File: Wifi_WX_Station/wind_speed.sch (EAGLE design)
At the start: 8 parts, among them T1 MMBT3904

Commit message: updated BOM with all prices- As Checked in to BATCH PCB
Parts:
- +5V, GND, OUT: value LSP10 -> TPSOL; device solpad:LSP10 -> wifi_WX:TPSOL
- OPTO1: device 1AA_Stofer:OSRAM_SHF9201 -> wifi_WX:OSRAM_SHF9201
- R1: device rcl:R-US_R0805 -> rcl:R-US_R0603
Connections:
- net N$2: now also GND.P$1; no longer GND.MP
- net N$3: now also +5V.P$1; no longer +5V.MP
- net N$4: now also OUT.P$1; no longer OUT.MP
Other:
- moved on the sheet: R1, R2, R3, T1
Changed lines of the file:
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@@
 </classes>
 <parts>
-<part name="OPTO1" library="1AA_Stofer" deviceset="OSRAM_SHF9201" device=""/>
+<part name="OPTO1" library="wifi_WX" deviceset="OSRAM_SHF9201" device=""/>
 <part name="T1" library="transistor" deviceset="BC846" device="" value="MMBT3904"/>
-<part name="R1" library="rcl" deviceset="R-US_" device="R0805" value="10K"/>
-<part name="+5V" library="solpad" deviceset="LSP10" device=""/>
-<part name="GND" library="solpad" deviceset="LSP10" device=""/>
-<part name="OUT" library="solpad" deviceset="LSP10" device=""/>
+<part name="R1" library="rcl" deviceset="R-US_" device="R0603" value="10K"/>
 <part name="R2" library="rcl" deviceset="R-US_" device="R0603" value="120o"/>
 <part name="R3" library="rcl" deviceset="R-US_" device="R0603" value="120o"/>
+<part name="+5V" library="wifi_WX" deviceset="TP" device="SOL"/>
+<part name="GND" library="wifi_WX" deviceset="TP" device="SOL"/>
+<part name="OUT" library="wifi_WX" deviceset="TP" device="SOL"/>
 </parts>
 <sheets>
@@
 </plain>
 <instances>
-<instance part="OPTO1" gate="G$1" x="101.6" y="60.96"/>
-<instance part="T1" gate="G$1" x="139.7" y="63.5"/>
-<instance part="R1" gate="G$1" x="116.84" y="81.28" rot="R90"/>
-<instance part="+5V" gate="1" x="83.82" y="88.9" rot="R90"/>
-<instance part="GND" gate="1" x="83.82" y="48.26" rot="R90"/>
-<instance part="OUT" gate="1" x="142.24" y="86.36"/>
-<instance part="R2" gate="G$1" x="91.44" y="83.82" rot="R90"/>
-<instance part="R3" gate="G$1" x="91.44" y="73.66" rot="R90"/>
+<instance part="OPTO1" gate="G$1" x="101.6" y="60.96" smashed="yes">
+<attribute name="NAME" x="99.06" y="63.5" size="1.27" layer="95"/>
+<attribute name="VALUE" x="96.52" y="50.8" size="1.27" layer="96"/>
+</instance>
+<instance part="T1" gate="G$1" x="124.46" y="71.12"/>
+<instance part="R1" gate="G$1" x="109.22" y="83.82" rot="R90"/>
+<instance part="R2" gate="G$1" x="96.52" y="91.44" rot="R90"/>
+<instance part="R3" gate="G$1" x="96.52" y="78.74" rot="R90"/>
+<instance part="+5V" gate="G$1" x="83.82" y="96.52"/>
+<instance part="GND" gate="G$1" x="83.82" y="48.26"/>
+<instance part="OUT" gate="G$1" x="132.08" y="96.52" rot="R180"/>
 </instances>
 <busses>
@@
 <pinref part="R1" gate="G$1" pin="1"/>
 <pinref part="OPTO1" gate="G$1" pin="C"/>
-<wire x1="116.84" y1="76.2" x2="116.84" y2="68.58" width="0.1524" layer="91"/>
-<wire x1="116.84" y1="68.58" x2="111.76" y2="68.58" width="0.1524" layer="91"/>
-<wire x1="111.76" y1="68.58" x2="124.46" y2="68.58" width="0.1524" layer="91"/>
-<wire x1="124.46" y1="68.58" x2="124.46" y2="63.5" width="0.1524" layer="91"/>
+<wire x1="109.22" y1="78.74" x2="109.22" y2="71.12" width="0.1524" layer="91"/>
+<wire x1="109.22" y1="71.12" x2="121.92" y2="71.12" width="0.1524" layer="91"/>
 <pinref part="T1" gate="G$1" pin="B"/>
-<wire x1="124.46" y1="63.5" x2="137.16" y2="63.5" width="0.1524" layer="91"/>
 </segment>
 </net>
@@
 <segment>
 <pinref part="OPTO1" gate="G$1" pin="E"/>
-<wire x1="111.76" y1="55.88" x2="111.76" y2="48.26" width="0.1524" layer="91"/>
+<wire x1="109.22" y1="53.34" x2="109.22" y2="48.26" width="0.1524" layer="91"/>
 <pinref part="T1" gate="G$1" pin="E"/>
-<wire x1="111.76" y1="48.26" x2="142.24" y2="48.26" width="0.1524" layer="91"/>
-<wire x1="142.24" y1="48.26" x2="142.24" y2="58.42" width="0.1524" layer="91"/>
+<wire x1="109.22" y1="48.26" x2="127" y2="48.26" width="0.1524" layer="91"/>
+<wire x1="127" y1="48.26" x2="127" y2="66.04" width="0.1524" layer="91"/>
 <pinref part="OPTO1" gate="G$1" pin="CATH"/>
-<wire x1="111.76" y1="48.26" x2="86.36" y2="48.26" width="0.1524" layer="91"/>
-<wire x1="86.36" y1="48.26" x2="86.36" y2="55.88" width="0.1524" layer="91"/>
-<wire x1="86.36" y1="55.88" x2="93.98" y2="55.88" width="0.1524" layer="91"/>
-<pinref part="GND" gate="1" pin="MP"/>
-<junction x="86.36" y="48.26"/>
+<wire x1="109.22" y1="48.26" x2="96.52" y2="48.26" width="0.1524" layer="91"/>
+<wire x1="88.9" y1="48.26" x2="96.52" y2="48.26" width="0.1524" layer="91"/>
+<wire x1="96.52" y1="48.26" x2="96.52" y2="53.34" width="0.1524" layer="91"/>
+<pinref part="GND" gate="G$1" pin="P$1"/>
 </segment>
 </net>
 <net name="N$3" class="0">
 <segment>
-<wire x1="86.36" y1="88.9" x2="91.44" y2="88.9" width="0.1524" layer="91"/>
+<wire x1="88.9" y1="96.52" x2="96.52" y2="96.52" width="0.1524" layer="91"/>
 <pinref part="R1" gate="G$1" pin="2"/>
-<wire x1="91.44" y1="88.9" x2="116.84" y2="88.9" width="0.1524" layer="91"/>
-<wire x1="116.84" y1="88.9" x2="116.84" y2="86.36" width="0.1524" layer="91"/>
-<pinref part="+5V" gate="1" pin="MP"/>
+<wire x1="96.52" y1="96.52" x2="109.22" y2="96.52" width="0.1524" layer="91"/>
+<wire x1="109.22" y1="96.52" x2="109.22" y2="88.9" width="0.1524" layer="91"/>
 <pinref part="R2" gate="G$1" pin="2"/>
+<pinref part="+5V" gate="G$1" pin="P$1"/>
 </segment>
 </net>
@@
 <segment>
 <pinref part="T1" gate="G$1" pin="C"/>
-<wire x1="142.24" y1="68.58" x2="142.24" y2="83.82" width="0.1524" layer="91"/>
-<pinref part="OUT" gate="1" pin="MP"/>
+<wire x1="127" y1="76.2" x2="127" y2="96.52" width="0.1524" layer="91"/>
+<pinref part="OUT" gate="G$1" pin="P$1"/>
 </segment>
 </net>
@@
 <segment>
 <pinref part="OPTO1" gate="G$1" pin="AN"/>
-<wire x1="91.44" y1="68.58" x2="93.98" y2="68.58" width="0.1524" layer="91"/>
+<wire x1="96.52" y1="73.66" x2="96.52" y2="71.12" width="0.1524" layer="91"/>
 <pinref part="R3" gate="G$1" pin="1"/>
 </segment>
@@
 <pinref part="R2" gate="G$1" pin="1"/>
 <pinref part="R3" gate="G$1" pin="2"/>
+<wire x1="96.52" y1="86.36" x2="96.52" y2="83.82" width="0.1524" layer="91"/>
 </segment>
 </net>

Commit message: Revision B.1
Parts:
- added R4: 1K, rcl:R-US_R0603
- added R5: 330, rcl:R-US_R0603
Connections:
- net N$3: now also R4.2
- net N$4: now also R4.1, R5.1
- net N$6: now also R5.2
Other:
- moved on the sheet: +5V, OUT, R1, R2, R3
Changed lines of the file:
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@@
 <part name="GND" library="wifi_WX" deviceset="TP" device="SOL"/>
 <part name="OUT" library="wifi_WX" deviceset="TP" device="SOL"/>
+<part name="R4" library="rcl" deviceset="R-US_" device="R0603" value="1K"/>
+<part name="R5" library="rcl" deviceset="R-US_" device="R0603" value="330"/>
 </parts>
 <sheets>
@@
 </instance>
 <instance part="T1" gate="G$1" x="124.46" y="71.12"/>
-<instance part="R1" gate="G$1" x="109.22" y="83.82" rot="R90"/>
-<instance part="R2" gate="G$1" x="96.52" y="91.44" rot="R90"/>
-<instance part="R3" gate="G$1" x="96.52" y="78.74" rot="R90"/>
-<instance part="+5V" gate="G$1" x="83.82" y="96.52"/>
+<instance part="R1" gate="G$1" x="109.22" y="96.52" rot="R90"/>
+<instance part="R2" gate="G$1" x="96.52" y="99.06" rot="R90"/>
+<instance part="R3" gate="G$1" x="96.52" y="76.2" rot="R90"/>
+<instance part="+5V" gate="G$1" x="83.82" y="104.14"/>
 <instance part="GND" gate="G$1" x="83.82" y="48.26"/>
-<instance part="OUT" gate="G$1" x="132.08" y="96.52" rot="R180"/>
+<instance part="OUT" gate="G$1" x="132.08" y="104.14" rot="R180"/>
+<instance part="R4" gate="G$1" x="116.84" y="104.14" rot="R180"/>
+<instance part="R5" gate="G$1" x="119.38" y="86.36" rot="R180"/>
 </instances>
 <busses>
@@
 <pinref part="R1" gate="G$1" pin="1"/>
 <pinref part="OPTO1" gate="G$1" pin="C"/>
-<wire x1="109.22" y1="78.74" x2="109.22" y2="71.12" width="0.1524" layer="91"/>
+<wire x1="109.22" y1="91.44" x2="109.22" y2="71.12" width="0.1524" layer="91"/>
 <wire x1="109.22" y1="71.12" x2="121.92" y2="71.12" width="0.1524" layer="91"/>
 <pinref part="T1" gate="G$1" pin="B"/>
@@
 <net name="N$3" class="0">
 <segment>
-<wire x1="88.9" y1="96.52" x2="96.52" y2="96.52" width="0.1524" layer="91"/>
+<wire x1="88.9" y1="104.14" x2="96.52" y2="104.14" width="0.1524" layer="91"/>
 <pinref part="R1" gate="G$1" pin="2"/>
-<wire x1="96.52" y1="96.52" x2="109.22" y2="96.52" width="0.1524" layer="91"/>
-<wire x1="109.22" y1="96.52" x2="109.22" y2="88.9" width="0.1524" layer="91"/>
+<wire x1="96.52" y1="104.14" x2="109.22" y2="104.14" width="0.1524" layer="91"/>
+<wire x1="109.22" y1="104.14" x2="109.22" y2="101.6" width="0.1524" layer="91"/>
 <pinref part="R2" gate="G$1" pin="2"/>
 <pinref part="+5V" gate="G$1" pin="P$1"/>
+<pinref part="R4" gate="G$1" pin="2"/>
+<wire x1="109.22" y1="104.14" x2="111.76" y2="104.14" width="0.1524" layer="91"/>
 </segment>
 </net>
@@
 <segment>
 <pinref part="T1" gate="G$1" pin="C"/>
-<wire x1="127" y1="76.2" x2="127" y2="96.52" width="0.1524" layer="91"/>
+<wire x1="127" y1="76.2" x2="127" y2="86.36" width="0.1524" layer="91"/>
 <pinref part="OUT" gate="G$1" pin="P$1"/>
+<pinref part="R4" gate="G$1" pin="1"/>
+<wire x1="127" y1="86.36" x2="127" y2="104.14" width="0.1524" layer="91"/>
+<wire x1="121.92" y1="104.14" x2="127" y2="104.14" width="0.1524" layer="91"/>
+<pinref part="R5" gate="G$1" pin="1"/>
+<wire x1="124.46" y1="86.36" x2="127" y2="86.36" width="0.1524" layer="91"/>
 </segment>
 </net>
@@
 <segment>
 <pinref part="OPTO1" gate="G$1" pin="AN"/>
-<wire x1="96.52" y1="73.66" x2="96.52" y2="71.12" width="0.1524" layer="91"/>
 <pinref part="R3" gate="G$1" pin="1"/>
 </segment>
@@
 <pinref part="R2" gate="G$1" pin="1"/>
 <pinref part="R3" gate="G$1" pin="2"/>
-<wire x1="96.52" y1="86.36" x2="96.52" y2="83.82" width="0.1524" layer="91"/>
+<wire x1="96.52" y1="93.98" x2="96.52" y2="86.36" width="0.1524" layer="91"/>
+<pinref part="R5" gate="G$1" pin="2"/>
+<wire x1="96.52" y1="86.36" x2="96.52" y2="81.28" width="0.1524" layer="91"/>
+<wire x1="114.3" y1="86.36" x2="96.52" y2="86.36" width="0.1524" layer="91"/>
 </segment>
 </net>

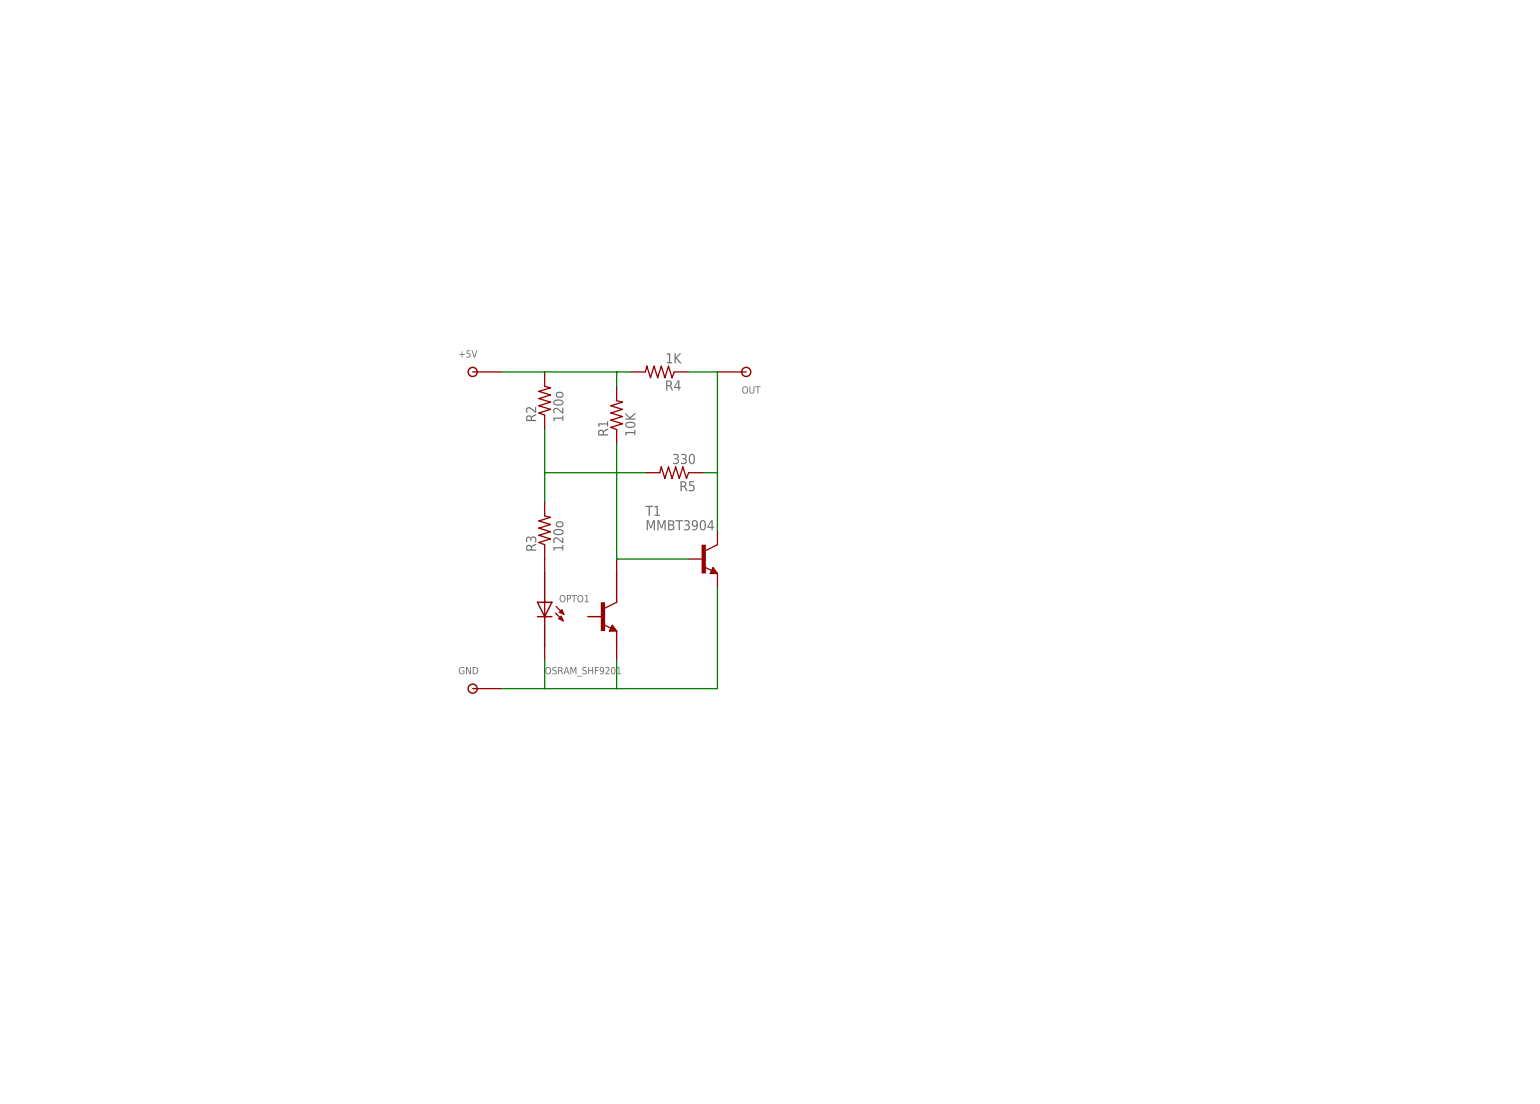
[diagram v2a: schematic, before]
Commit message: added SILabs Hygrometer board Added frames to the schematics
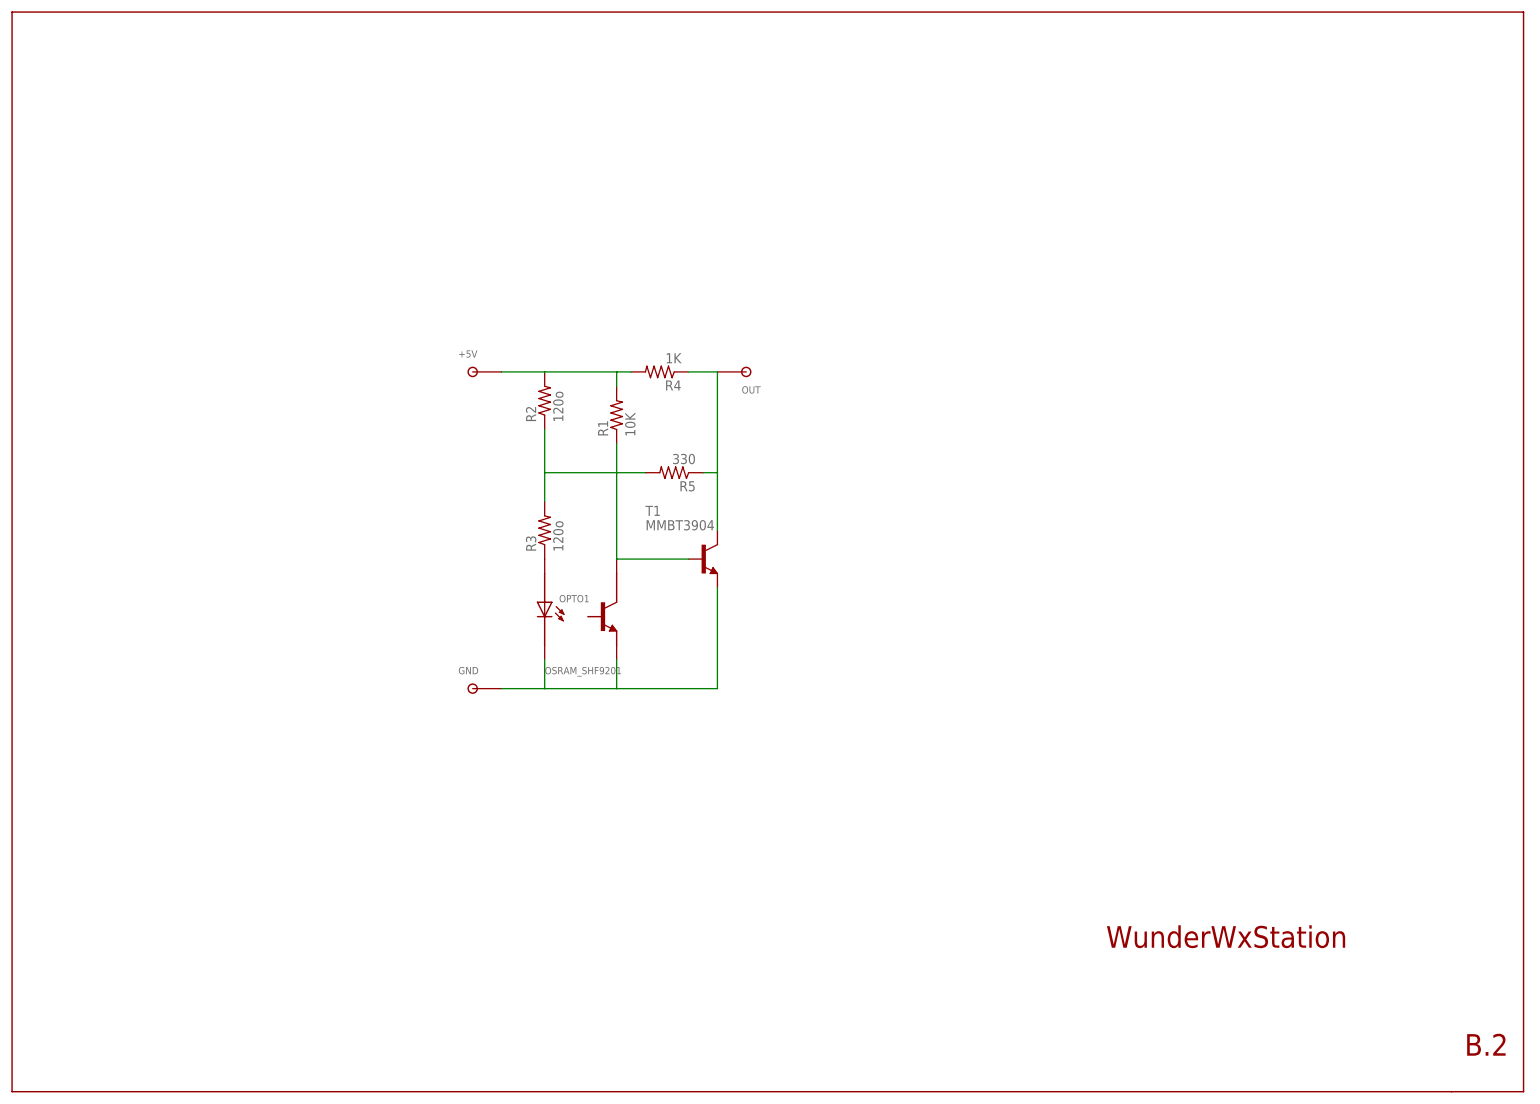
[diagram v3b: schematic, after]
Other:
- note added: "B.2"
- note added: "WunderWxStation"
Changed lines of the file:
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@@
 <grid distance="0.1" unitdist="inch" unit="inch" style="lines" multiple="1" display="no" altdistance="0.01" altunitdist="inch" altunit="inch"/>
 <layers>
-<layer number="1" name="Top" color="4" fill="1" visible="yes" active="no"/>
-<layer number="16" name="Bottom" color="1" fill="1" visible="yes" active="no"/>
-<layer number="17" name="Pads" color="2" fill="1" visible="yes" active="no"/>
-<layer number="18" name="Vias" color="2" fill="1" visible="yes" active="no"/>
-<layer number="19" name="Unrouted" color="6" fill="1" visible="yes" active="no"/>
-<layer number="20" name="Dimension" color="15" fill="1" visible="yes" active="no"/>
-<layer number="21" name="tPlace" color="7" fill="1" visible="yes" active="no"/>
-<layer number="22" name="bPlace" color="7" fill="1" visible="yes" active="no"/>
-<layer number="23" name="tOrigins" color="15" fill="1" visible="yes" active="no"/>
-<layer number="24" name="bOrigins" color="15" fill="1" visible="yes" active="no"/>
-<layer number="25" name="tNames" color="7" fill="1" visible="yes" active="no"/>
-<layer number="26" name="bNames" color="7" fill="1" visible="yes" active="no"/>
-<layer number="27" name="tValues" color="7" fill="1" visible="yes" active="no"/>
-<layer number="28" name="bValues" color="7" fill="1" visible="yes" active="no"/>
+<layer number="1" name="Top" color="4" fill="1" visible="no" active="no"/>
+<layer number="16" name="Bottom" color="1" fill="1" visible="no" active="no"/>
+<layer number="17" name="Pads" color="2" fill="1" visible="no" active="no"/>
+<layer number="18" name="Vias" color="2" fill="1" visible="no" active="no"/>
+<layer number="19" name="Unrouted" color="6" fill="1" visible="no" active="no"/>
+<layer number="20" name="Dimension" color="15" fill="1" visible="no" active="no"/>
+<layer number="21" name="tPlace" color="7" fill="1" visible="no" active="no"/>
+<layer number="22" name="bPlace" color="7" fill="1" visible="no" active="no"/>
+<layer number="23" name="tOrigins" color="15" fill="1" visible="no" active="no"/>
+<layer number="24" name="bOrigins" color="15" fill="1" visible="no" active="no"/>
+<layer number="25" name="tNames" color="7" fill="1" visible="no" active="no"/>
+<layer number="26" name="bNames" color="7" fill="1" visible="no" active="no"/>
+<layer number="27" name="tValues" color="7" fill="1" visible="no" active="no"/>
+<layer number="28" name="bValues" color="7" fill="1" visible="no" active="no"/>
 <layer number="29" name="tStop" color="7" fill="3" visible="no" active="no"/>
 <layer number="30" name="bStop" color="7" fill="6" visible="no" active="no"/>
@@
 <layer number="35" name="tGlue" color="7" fill="4" visible="no" active="no"/>
 <layer number="36" name="bGlue" color="7" fill="5" visible="no" active="no"/>
-<layer number="37" name="tTest" color="7" fill="1" visible="yes" active="no"/>
-<layer number="38" name="bTest" color="7" fill="1" visible="yes" active="no"/>
+<layer number="37" name="tTest" color="7" fill="1" visible="no" active="no"/>
+<layer number="38" name="bTest" color="7" fill="1" visible="no" active="no"/>
 <layer number="39" name="tKeepout" color="4" fill="11" visible="no" active="no"/>
 <layer number="40" name="bKeepout" color="1" fill="11" visible="no" active="no"/>
@@
 <layer number="44" name="Drills" color="7" fill="1" visible="no" active="no"/>
 <layer number="45" name="Holes" color="7" fill="1" visible="no" active="no"/>
-<layer number="46" name="Milling" color="3" fill="1" visible="yes" active="no"/>
-<layer number="47" name="Measures" color="7" fill="1" visible="yes" active="no"/>
-<layer number="48" name="Document" color="7" fill="1" visible="yes" active="no"/>
-<layer number="49" name="Reference" color="7" fill="1" visible="yes" active="no"/>
-<layer number="50" name="dxf" color="7" fill="1" visible="yes" active="no"/>
-<layer number="51" name="tDocu" color="7" fill="1" visible="yes" active="no"/>
-<layer number="52" name="bDocu" color="7" fill="1" visible="yes" active="no"/>
-<layer number="53" name="tGND_GNDA" color="7" fill="9" visible="yes" active="no"/>
-<layer number="54" name="bGND_GNDA" color="1" fill="9" visible="yes" active="no"/>
-<layer number="56" name="wert" color="7" fill="1" visible="yes" active="no"/>
+<layer number="46" name="Milling" color="3" fill="1" visible="no" active="no"/>
+<layer number="47" name="Measures" color="7" fill="1" visible="no" active="no"/>
+<layer number="48" name="Document" color="7" fill="1" visible="no" active="no"/>
+<layer number="49" name="Reference" color="7" fill="1" visible="no" active="no"/>
+<layer number="50" name="dxf" color="7" fill="1" visible="no" active="no"/>
+<layer number="51" name="tDocu" color="7" fill="1" visible="no" active="no"/>
+<layer number="52" name="bDocu" color="7" fill="1" visible="no" active="no"/>
+<layer number="53" name="tGND_GNDA" color="7" fill="9" visible="no" active="no"/>
+<layer number="54" name="bGND_GNDA" color="1" fill="9" visible="no" active="no"/>
+<layer number="56" name="wert" color="7" fill="1" visible="no" active="no"/>
 <layer number="91" name="Nets" color="2" fill="1" visible="yes" active="yes"/>
 <layer number="92" name="Busses" color="1" fill="1" visible="yes" active="yes"/>
@@
 <part name="R4" library="rcl" deviceset="R-US_" device="R0603" value="1K"/>
 <part name="R5" library="rcl" deviceset="R-US_" device="R0603" value="330"/>
+<part name="U$1" library="1AA_Stofer" deviceset="8.5X11" device=""/>
 </parts>
 <sheets>
 <sheet>
 <plain>
+<text x="195.58" y="2.54" size="3.81" layer="94" ratio="20">WunderWxStation</text>
+<text x="258.826" y="-16.51" size="3.81" layer="94" ratio="20">B.2</text>
 </plain>
 <instances>
@@
 <instance part="R4" gate="G$1" x="116.84" y="104.14" rot="R180"/>
 <instance part="R5" gate="G$1" x="119.38" y="86.36" rot="R180"/>
+<instance part="U$1" gate="G$1" x="2.54" y="-22.86"/>
+<instance part="U$1" gate="G$2" x="167.64" y="-22.86"/>
 </instances>
 <busses>
